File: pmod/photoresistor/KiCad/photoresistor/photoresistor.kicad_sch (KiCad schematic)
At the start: 3 parts, among them J2 Conn_01x06_Pin

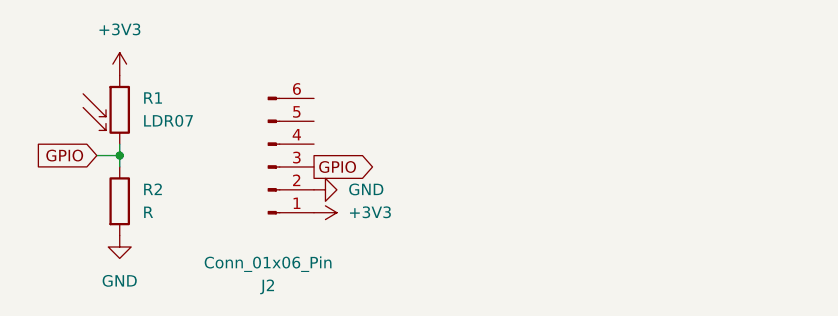
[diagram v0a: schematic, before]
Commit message: minor fixes and mounting hole added
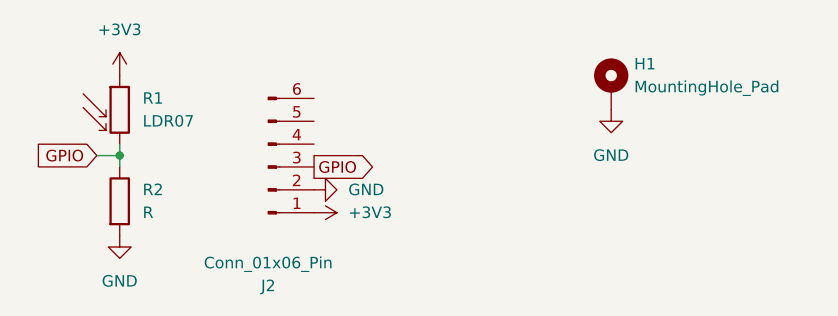
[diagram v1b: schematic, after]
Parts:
- added H1: MountingHole_Pad, symbol Mechanical:MountingHole_Pad
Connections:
- net GND: now also H1.1
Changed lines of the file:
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@@
+	(symbol
+		(lib_id "power:GND")
+		(at 133.35 71.12 0)
+		(unit 1)
+		(exclude_from_sim no)
+		(in_bom yes)
+		(on_board yes)
+		(dnp no)
+		(fields_autoplaced yes)
+		(property "Reference" "#PWR05"
+			(at 133.35 77.47 0)
+			(effects
+				(font
+					(size 1.27 1.27)
+				)
+				(hide yes)
+			)
+		)
+		(property "Value" "GND"
+			(at 133.35 76.2 0)
+			(effects
+				(font
+					(size 1.27 1.27)
+				)
+			)
+		)
+		(property "Footprint" ""
+			(at 133.35 71.12 0)
+			(effects
+				(font
+					(size 1.27 1.27)
+				)
+				(hide yes)
+			)
+		)
+		(property "Datasheet" ""
+			(at 133.35 71.12 0)
+			(effects
+				(font
+					(size 1.27 1.27)
+				)
+				(hide yes)
+			)
+		)
+		(property "Description" "Power symbol creates a global label with name \"GND\" , ground"
+			(at 133.35 71.12 0)
+			(effects
+				(font
+					(size 1.27 1.27)
+				)
+				(hide yes)
+			)
+		)
+		(pin "1"
+		)
+		(instances
+			(project ""
+				(path "/2ba0d2e0-9ec4-4fc9-abf2-81c0be384cdf"
+					(reference "#PWR05")
+					(unit 1)
+				)
+			)
+		)
+	)
 	(symbol
 		(lib_id "power:GND")
@@
 					(unit 1)
 				)
+			)
+		)
+	)
+	(symbol
+		(lib_id "Mechanical:MountingHole_Pad")
+		(at 133.35 68.58 0)
+		(unit 1)
+		(exclude_from_sim yes)
+		(in_bom no)
+		(on_board yes)
+		(dnp no)
+		(fields_autoplaced yes)
+		(property "Reference" "H1"
+			(at 135.89 66.0399 0)
+			(effects
+				(font
+					(size 1.27 1.27)
+				)
+				(justify left)
+			)
+		)
+		(property "Value" "MountingHole_Pad"
+			(at 135.89 68.5799 0)
+			(effects
+				(font
+					(size 1.27 1.27)
+				)
+				(justify left)
+			)
+		)
+		(property "Footprint" ""
+			(at 133.35 68.58 0)
+			(effects
+				(font
+					(size 1.27 1.27)
+				)
+				(hide yes)
+			)
+		)
+		(property "Datasheet" "~"
+			(at 133.35 68.58 0)
+			(effects
+				(font
+					(size 1.27 1.27)
+				)
+				(hide yes)
+			)
+		)
+		(property "Description" "Mounting Hole with connection"
+			(at 133.35 68.58 0)
+			(effects
+				(font
+					(size 1.27 1.27)
+				)
+				(hide yes)
+			)
+		)
+		(pin "1"
+		)
+		(instances
+			(project ""
+				(path "/2ba0d2e0-9ec4-4fc9-abf2-81c0be384cdf"
+					(reference "H1")
+					(unit 1)
+				)
